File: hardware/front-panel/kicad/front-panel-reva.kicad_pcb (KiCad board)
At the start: 2 copper layers, 35 parts, among them J1 UI_LINK / IDC 2x8 2.54mm, U1 TCA9534PWR

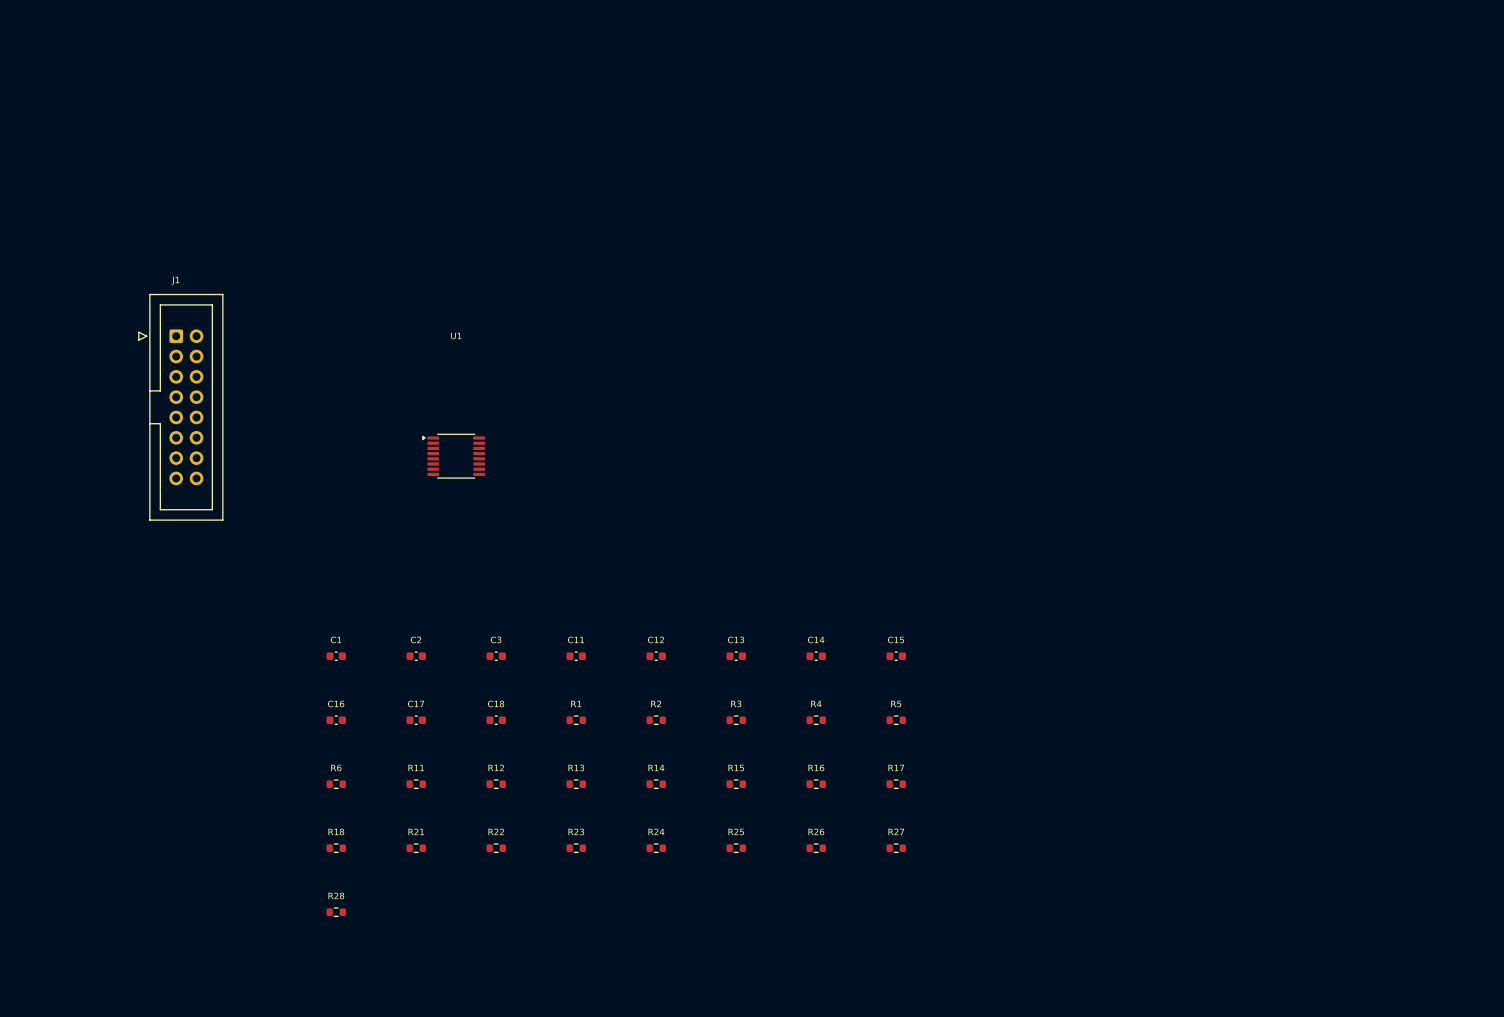
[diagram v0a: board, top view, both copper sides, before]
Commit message: Apply front panel mechanics to the KiCad PCB
Add the owner-accepted outline and four 8.4 mm milled holes as Edge.Cuts,
and the original switch, DL1, SP1-SP3 and JP3 positions as Dwgs.User
references. Move J1 and U1 to the off-board staging area. The new
apply_front_panel_mechanics.py edits the KiCad 10 text without pcbnew and
is idempotent; sync_front_panel_pcb.py now requires this outline. KiCad
DRC still has to be rerun.

Co-Authored-By: Claude Opus 5 <noreply@anthropic.com>
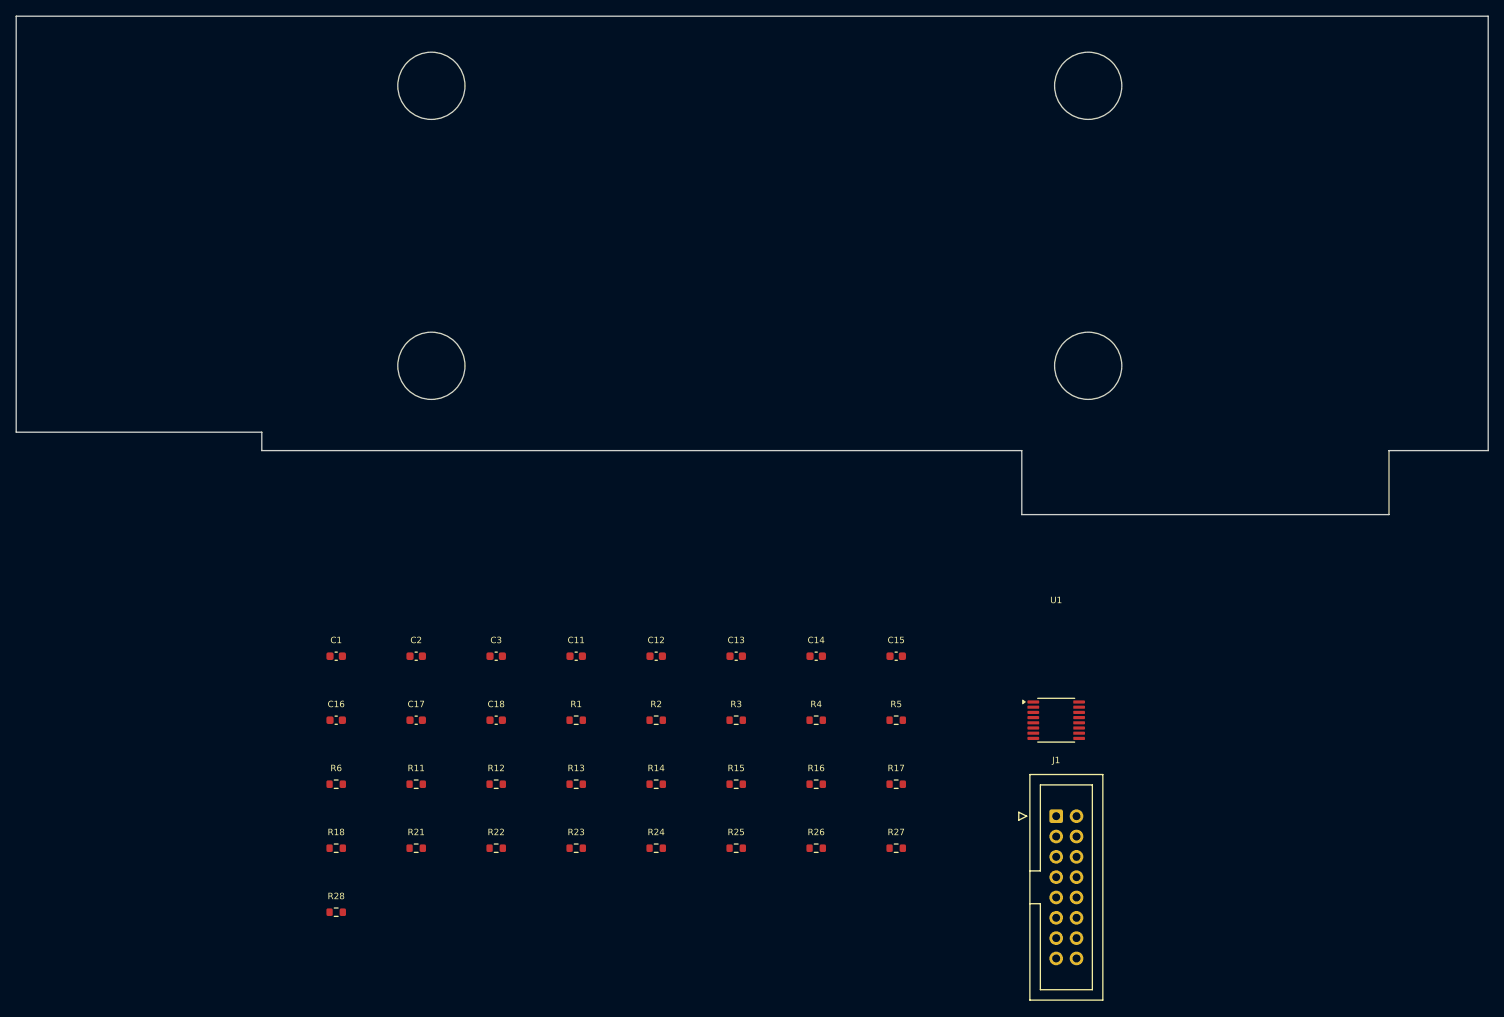
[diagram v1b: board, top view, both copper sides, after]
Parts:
- moved J1 125.3 mm to (130.0, 100.0)
- moved U1 81.9 mm to (130.0, 88.0)
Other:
- board outline added: 184 x 62.3 mm
- board text added: "DL1 orig."
- board text added: "JP3 orig. (+/-1 mm)"
- board text added: "MH1 Ø8.4 NPTH"
- board text added: "MH2 Ø8.4 NPTH"
- board text added: "MH3 Ø8.4 NPTH"
- board text added: "MH4 Ø8.4 NPTH"
- board text added: "PB1 (19.2, 9.9)"
- board text added: "PB2 (19.2, 25.6)"
- board text added: "PB3 (19.2, 41.2)"
- board text added: "PB4/PB6 (164.6, 41.2)"
- board text added: "PB5 (164.6, 25.6)"
- board text added: "PB7 (164.6, 9.9)"
- board text added: "PB8 (91.7, 43.5)"
- board text added: "SP1 TBD"
- board text added: "SP2 TBD"
- board text added: "SP3 TBD"
- board text added: "UNROUTED COMPONENT STAGING / NOT FOR FABRICATION Rev A outline + 8.4 mm holes accepted 2026-09-18 (photo-derived, +/-0.3 mm); switch references on Dwgs.User"
- board text removed: "UNROUTED COMPONENT STAGING / NOT FOR FABRICATION No outline; connector footprints and mechanical dimensions pending"
